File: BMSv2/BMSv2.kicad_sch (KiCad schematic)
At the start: 126 parts, among them J2 Conn_01x04_Socket, J3 Conn_01x02_Pin, J4 Conn_01x02_Pin, J5 Conn_01x03_Pin, Q1 AO3401A, SW1 SW_BOOT0, U1 STM32F405RGTx, U2 MCP2561-E-SN, U4 MP2332H, U5 AMS1117-3.3

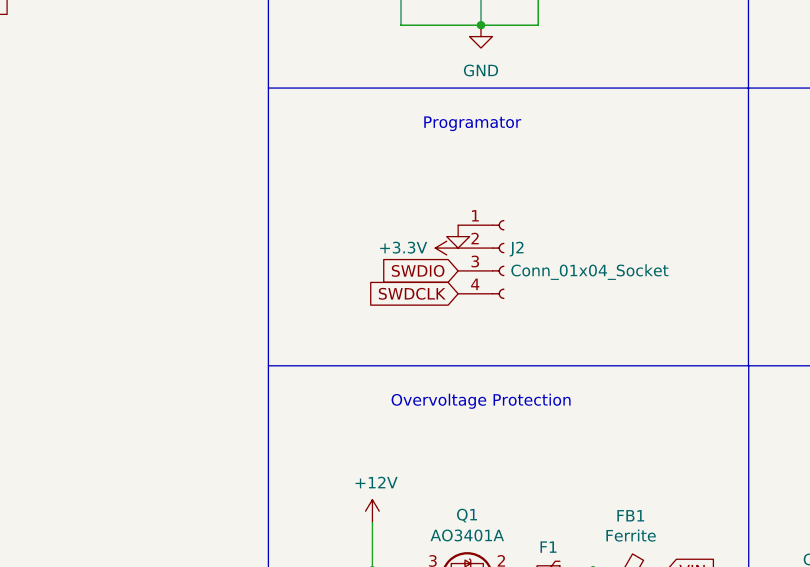
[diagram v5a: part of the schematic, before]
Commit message: GND connected
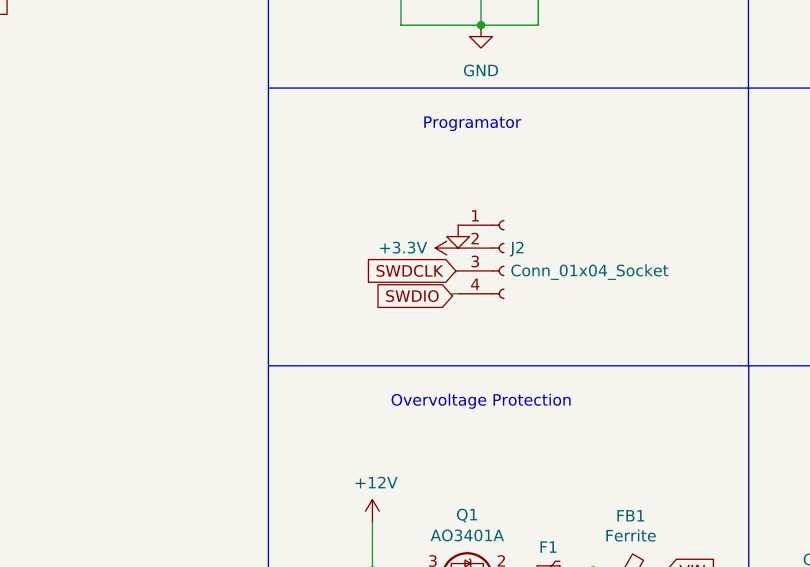
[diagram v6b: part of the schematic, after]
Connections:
- net SWDCLK: now also J2.3 (Pin_3); no longer J2.4 (Pin_4)
- net SWDIO: now also J2.4 (Pin_4); no longer J2.3 (Pin_3)
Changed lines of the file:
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@@
+    (stroke (width 0) (type default))
+  )
+  (wire (pts (xy 140.589 88.646) (xy 141.224 88.646))
     (stroke (width 0) (type default))
   )
@@
     (stroke (width 0) (type default))
   )
+  (wire (pts (xy 140.97 86.233) (xy 140.97 86.106))
+    (stroke (width 0) (type default))
+  )
   (wire (pts (xy 363.22 78.105) (xy 363.22 76.835))
     (stroke (width 0) (type default))
@@
     (stroke (width 0) (type default))
   )
+  (wire (pts (xy 140.589 88.9) (xy 140.589 88.646))
+    (stroke (width 0) (type default))
+  )
   (wire (pts (xy 167.386 181.61) (xy 167.386 184.15))
     (stroke (width 0) (type default))
@@
   )
   (wire (pts (xy 121.412 190.5) (xy 121.412 193.04))
+    (stroke (width 0) (type default))
+  )
+  (wire (pts (xy 140.97 86.106) (xy 141.224 86.106))
     (stroke (width 0) (type default))
   )
@@
     )
   )
-  (global_label "SWDCLK" (shape input) (at 141.224 88.646 180) (fields_autoplaced)
+  (global_label "SWDCLK" (shape input) (at 140.97 86.106 180) (fields_autoplaced)
     (effects (font (size 1.27 1.27)) (justify right))
-    (property "Intersheetrefs" "${INTERSHEET_REFS}" (at 130.7398 88.646 0)
+    (property "Intersheetrefs" "${INTERSHEET_REFS}" (at 130.4858 86.106 0)
       (effects (font (size 1.27 1.27)) (justify right) hide)
     )
@@
     )
   )
-  (global_label "SWDIO" (shape input) (at 141.224 86.106 180) (fields_autoplaced)
+  (global_label "SWDIO" (shape input) (at 140.589 88.9 180) (fields_autoplaced)
     (effects (font (size 1.27 1.27)) (justify right))
-    (property "Intersheetrefs" "${INTERSHEET_REFS}" (at 132.3726 86.106 0)
+    (property "Intersheetrefs" "${INTERSHEET_REFS}" (at 131.7376 88.9 0)
       (effects (font (size 1.27 1.27)) (justify right) hide)
     )

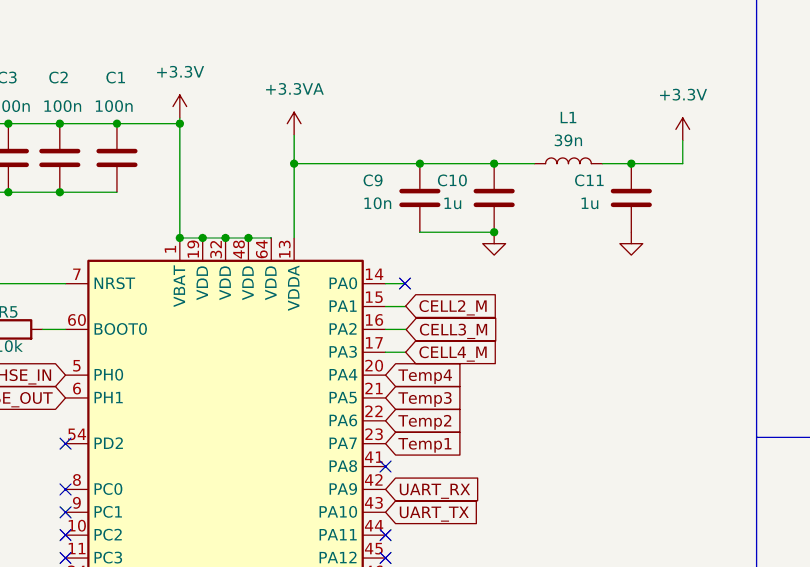
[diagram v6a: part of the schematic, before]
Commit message: added BOM and changed Vias
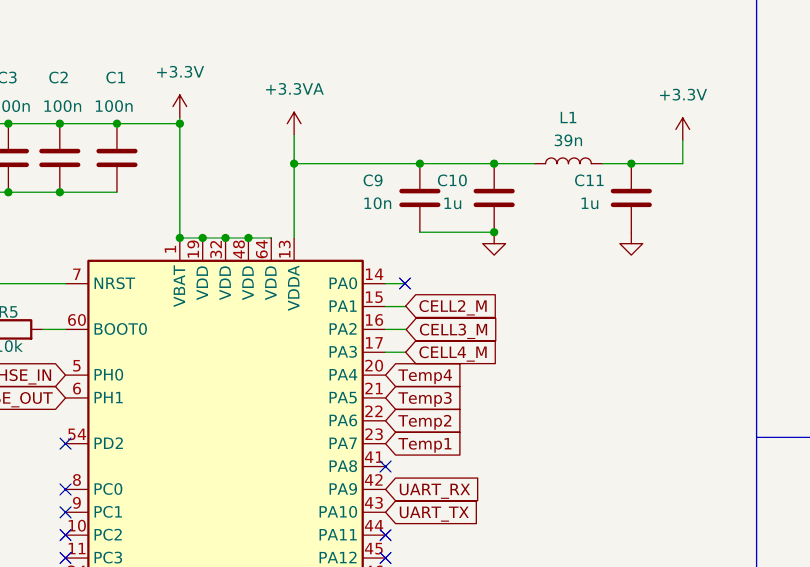
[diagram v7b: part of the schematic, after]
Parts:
- Y?: footprint footprints:Kryształ_16MHz_BMS -> footprints:XTAL_ECS-160-10-37-JTN-TR
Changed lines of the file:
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@@
   (no_connect (at 43.3585 79.1965))
   (no_connect (at 43.3585 66.4965))
-  (no_connect (at 81.0768 48.701))
+  (no_connect (at 81.0768 48.6918))
   (no_connect (at 43.3585 91.8965))
   (no_connect (at 78.9185 117.2965))
@@
       (effects (font (size 1.27 1.27)))
     )
-    (property "Footprint" "footprints:Kryształ_16MHz_BMS" (at 141.224 34.671 0)
+    (property "Footprint" "footprints:XTAL_ECS-160-10-37-JTN-TR" (at 141.224 34.671 0)
       (effects (font (size 1.27 1.27)) hide)
     )

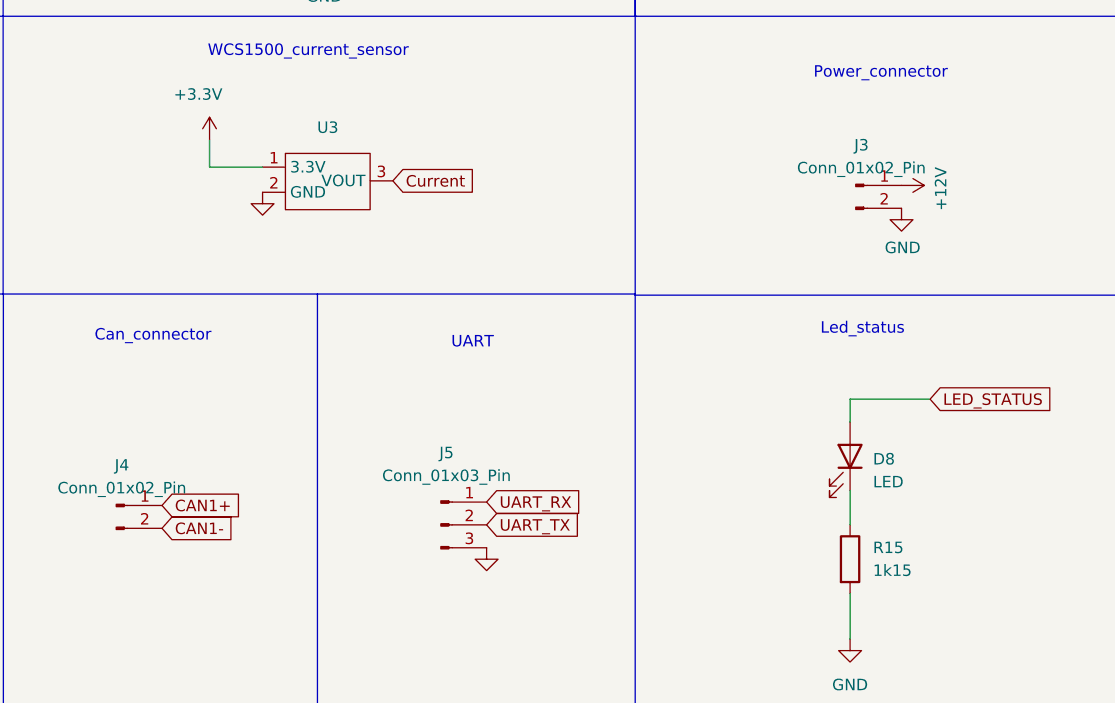
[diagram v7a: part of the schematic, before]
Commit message: added PGR slikscreen and export gerber files
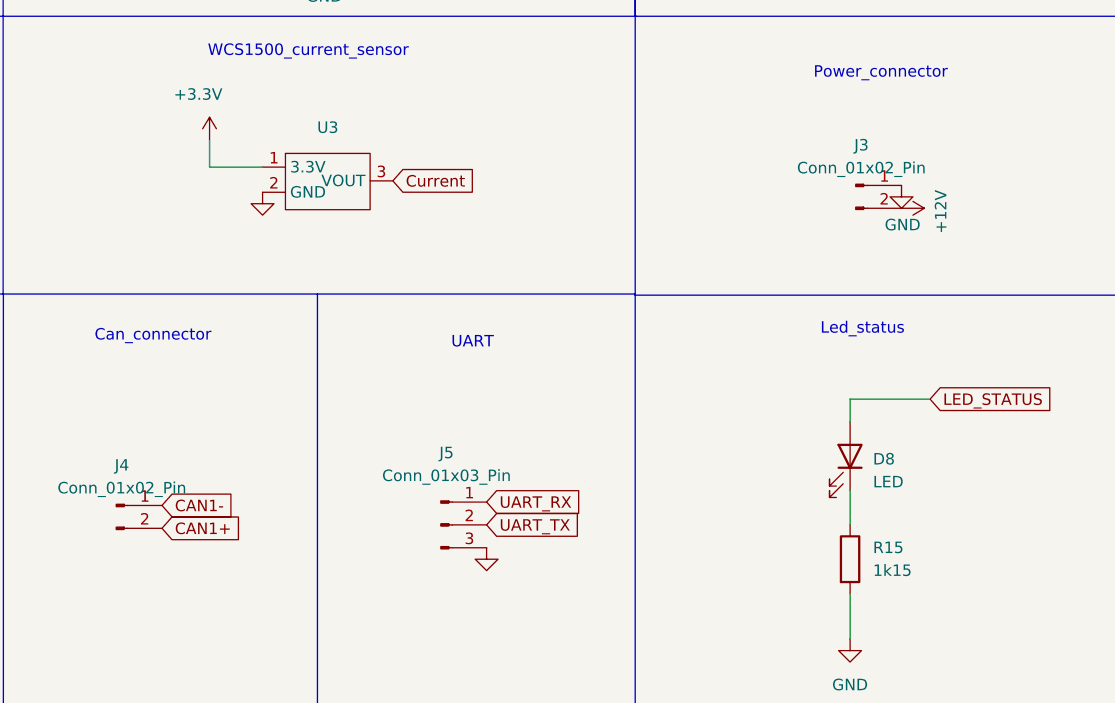
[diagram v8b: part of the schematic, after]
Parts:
- J3: footprint Connector_Molex:Molex_KK-254_AE-6410-02A_1x02_P2.54mm_Vertical -> Connector_Molex:Molex_PicoBlade_53048-0210_1x02_P1.25mm_Horizontal
- J4: footprint Connector_Molex:Molex_KK-254_AE-6410-02A_1x02_P2.54mm_Vertical -> Connector_Molex:Molex_PicoBlade_53261-0271_1x02-1MP_P1.25mm_Horizontal
- J?: footprint Connector_JST:JST_EH_S5B-EH_1x05_P2.50mm_Horizontal -> Connector_JST:JST_XH_S5B-XH-A_1x05_P2.50mm_Horizontal
- R?: value R -> 3k
- R? (x4): value R -> 30
- R? (x3): value R -> 120
- R? (x10): value R -> 1k
- R? (x4): value R -> 620
- R?: value R -> 500
- R?: value TC -> 120
- R? (x2): value R -> 2k
- R?: value R -> 1.5k
- R?: value R -> 4300
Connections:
- net +12V: now also J3.2 (Pin_2); no longer J3.1 (Pin_1)
- net CAN1+: now also J4.2 (Pin_2); no longer J4.1 (Pin_1)
- net CAN1-: now also J4.1 (Pin_1); no longer J4.2 (Pin_2)
- net GND: now also J3.1 (Pin_1); no longer J3.2 (Pin_2)
